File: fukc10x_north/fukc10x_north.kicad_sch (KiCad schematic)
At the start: 29 parts, among them J1 SM04B-SRSS-TB, J2 LED_Conn01x02_Pin, J3 LED_Conn01x02_Pin, J4 LED_Conn01x02_Pin, J5 LED_Conn01x02_Pin, J6 LED_Conn01x02_Pin, J7 LED_Conn01x02_Pin, J8 LED_Conn01x02_Pin, U1 XC6206P332MR, U2 STM32F072CBT6

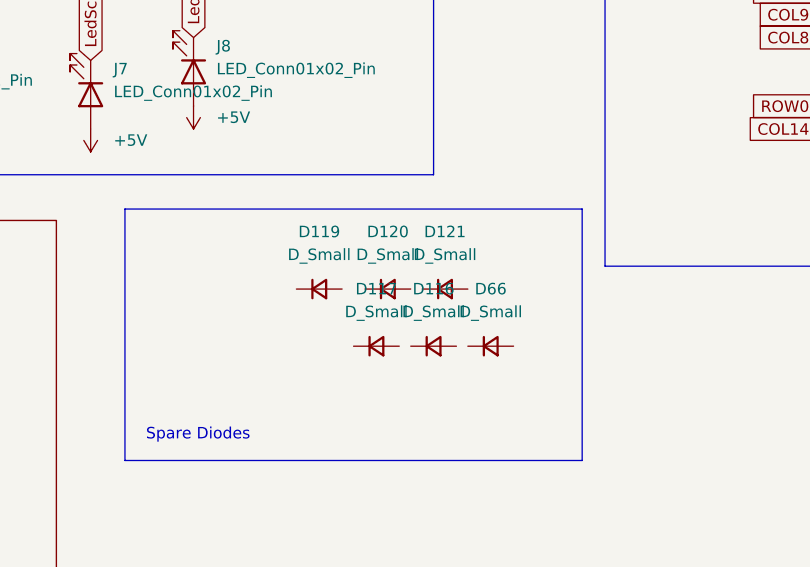
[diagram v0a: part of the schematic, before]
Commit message: updated parts for bom and stuff
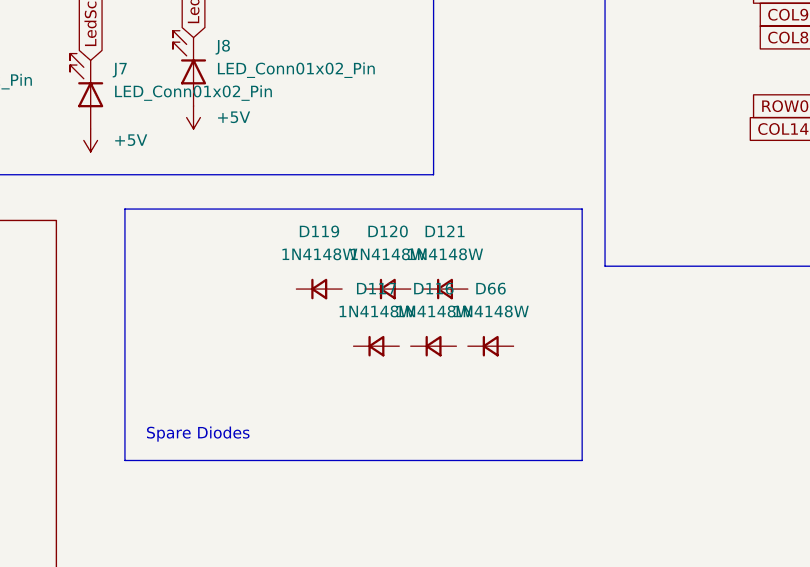
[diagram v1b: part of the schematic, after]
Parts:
- C10: MPN (none) -> CL05B104KO5NNNC
- D116, D117, D119, D120, D121, D66: value D_Small -> 1N4148W
- J2, J3, J4, J5, J6, J7, J8: now left out of the parts list

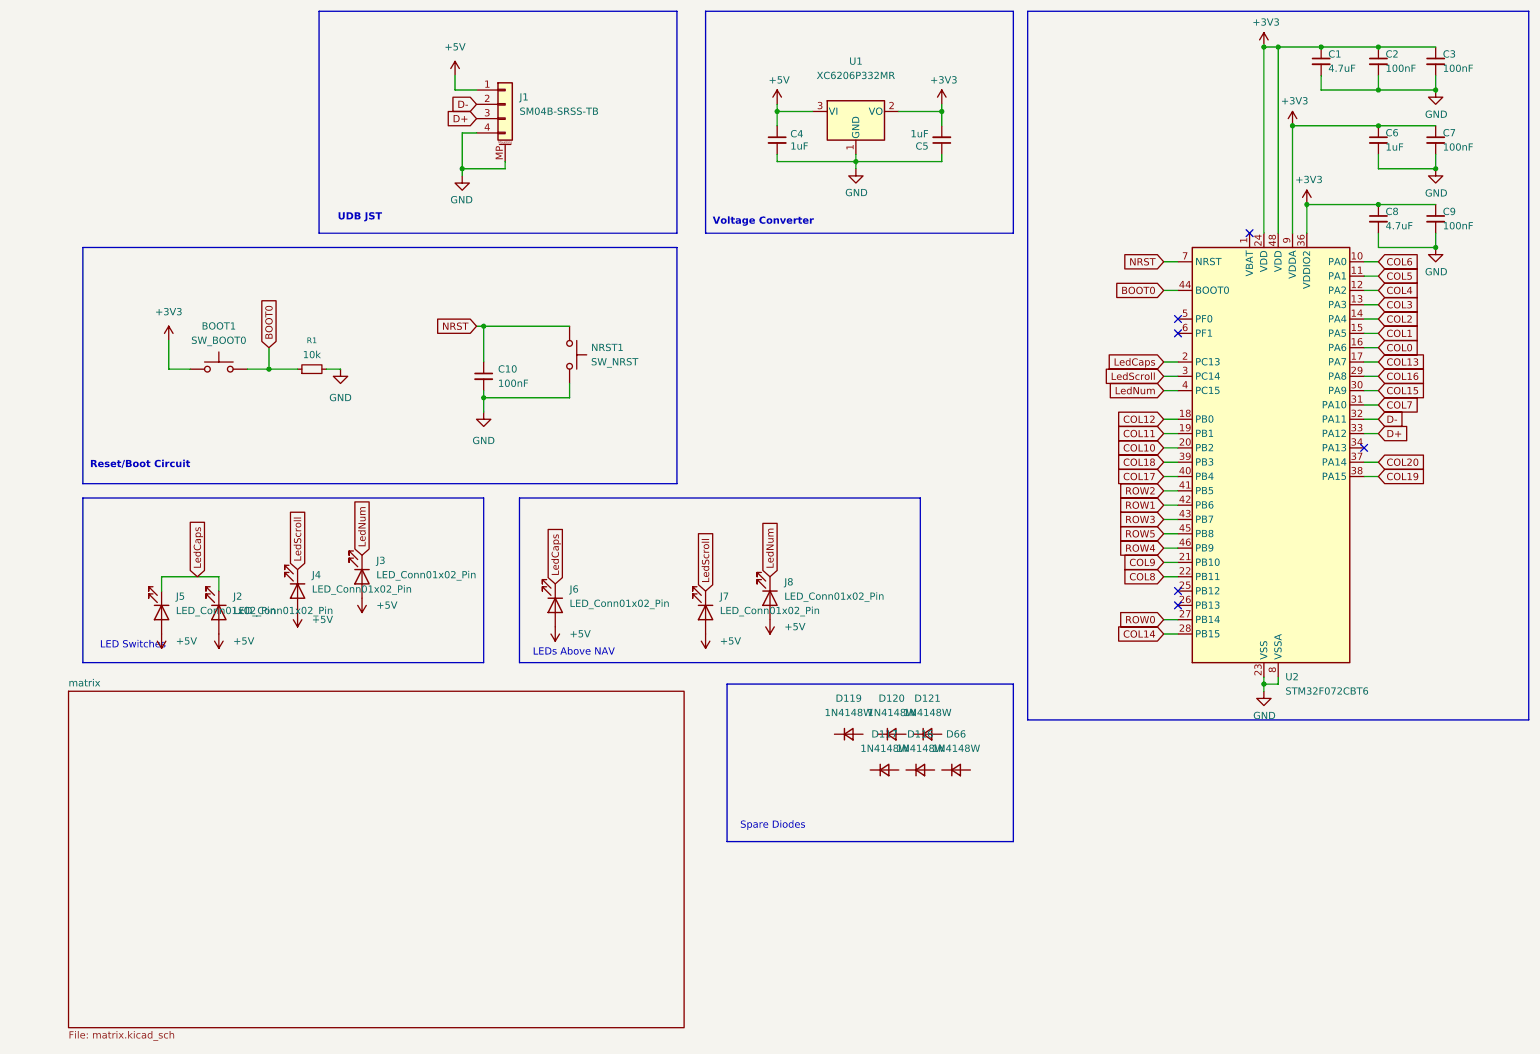
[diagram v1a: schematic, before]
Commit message: After feedback from gondo draining resistors and a crowbar diode added. Symbol for mcu changed to one from acheron project. Power/ground planes adjusted and added island around MCU for power and ground. Rerouted diodes adjusted trace widths.
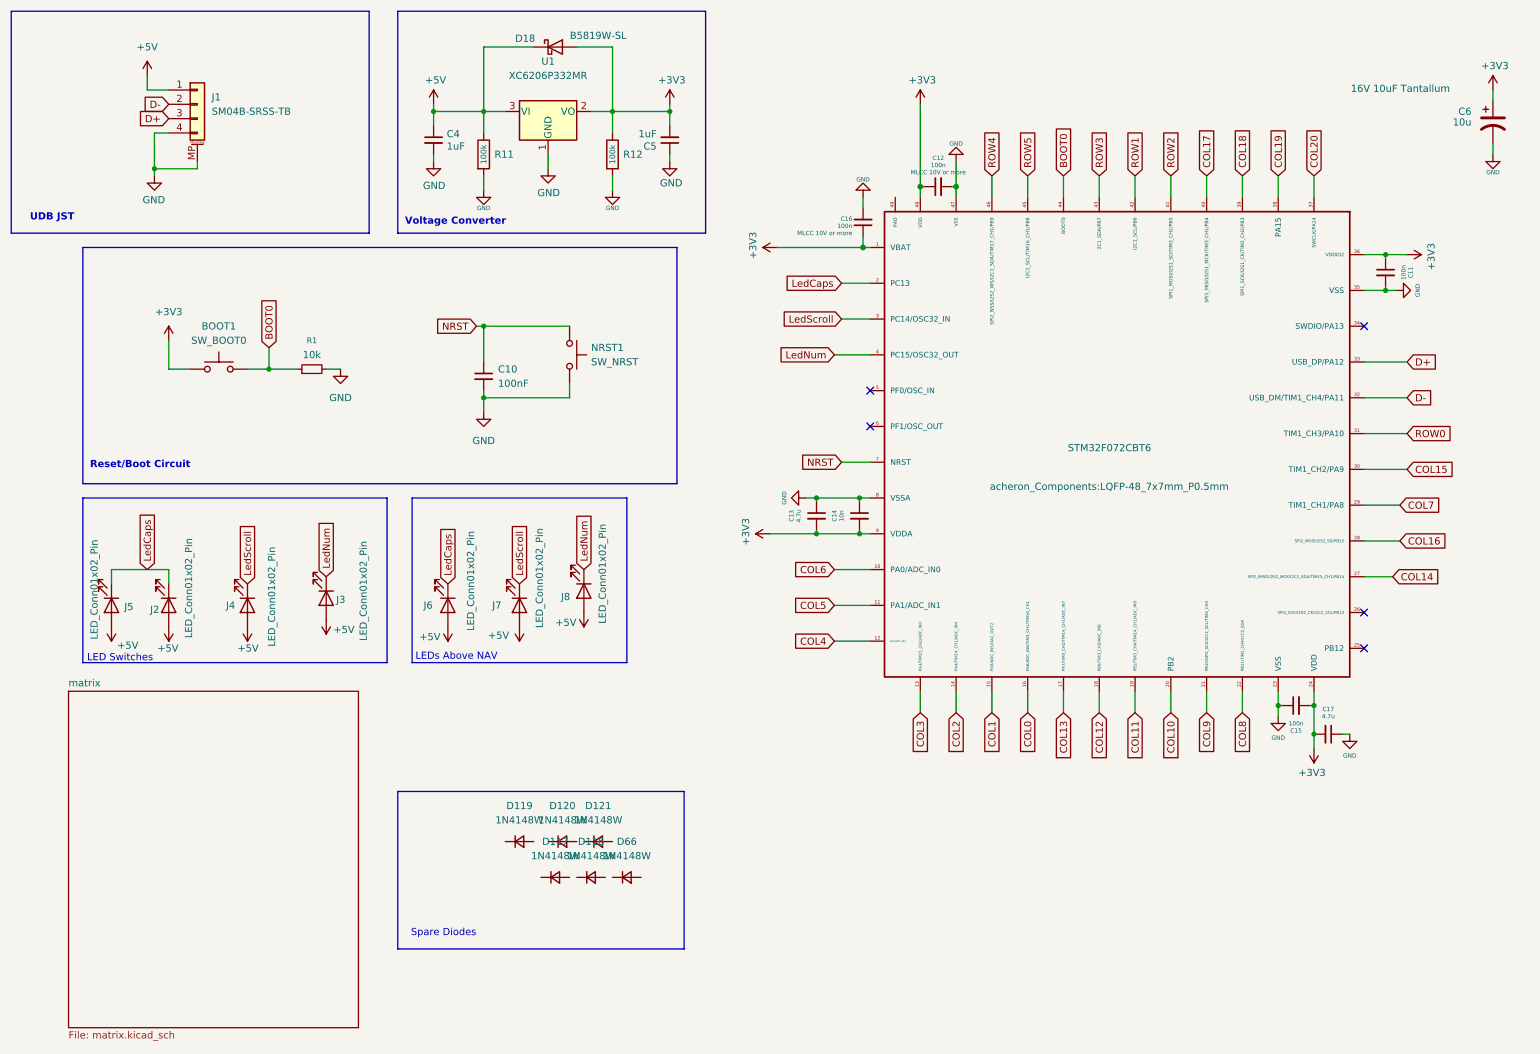
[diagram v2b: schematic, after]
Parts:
- removed C1, C8: 4.7uF, Capacitor_SMD:C_0402_1005Metric, symbol Device:C_Small
- removed C2, C3, C7, C9: 100nF, Capacitor_SMD:C_0402_1005Metric, symbol Device:C_Small
- removed C6: 1uF, Capacitor_SMD:C_0402_1005Metric, symbol Device:C_Small
- added C11, C12, C15, C16: 100n, Capacitor_SMD:C_0402_1005Metric, symbol Device:C_Small
- added C13, C17: 4.7u, Capacitor_SMD:C_0402_1005Metric, symbol Device:C_Small
- added C14: 10n, Capacitor_SMD:C_0402_1005Metric, symbol Device:C_Small
- added C6: 10u, acheron_Components:CP_EIA-3216-10_Kemet-I_Pad1.58x1.35mm_HandSolder, symbol Device:CP1
- added D18: B5819W-SL, acheron_Components:D_SOD-123, symbol Device:D_Schottky
- added R11, R12: 100k, Resistor_SMD:R_0805_2012Metric, symbol Device:R
- U2: footprint Package_QFP:LQFP-48_7x7mm_P0.5mm -> acheron_Components:LQFP-48_7x7mm_P0.5mm; symbol MCU_ST_STM32F0:STM32F072C8Tx -> Alexandria Acheron:STM32F072-UFQFPN48
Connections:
- net +3V3: now also U2.1 (VBAT), C11.1, C12.1, C13.2, C14.2, C15.2, C16.1, C17.2, C6.1, D18.2 (A), R12.1
- net +5V: now also D18.1 (K), R11.1
- net COL14: now also U2.27 (SPI2_MISO/I2S2_MCK/I2C2_SDA/TIM15_CH1/PB14); no longer U2.28 (PB15)
- net COL16: now also U2.28 (SPI2_MOSI/I2S2_SD/PB15); no longer U2.29 (PA8)
- net COL7: now also U2.29 (TIM1_CH1/PA8); no longer U2.31 (PA10)
- net GND: now also C11.2, C12.2, C13.1, C14.1, C15.1, C16.2, C17.1, C6.2, R11.2, R12.2
- net ROW0: now also U2.31 (TIM1_CH3/PA10); no longer U2.27 (PB14)
- no-connect marks 6 -> 5
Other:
- moved on the sheet: C4, C5, D116, D117, D119, D120, D121, D66, J1, J2, J3, J4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

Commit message: added library, fixed some routing and LED stuff
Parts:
- added Q1: AO3401A, acheron_Components:SOT-23, symbol Transistor_FET:AO3401A
- added Q2, Q3, Q4, Q5: 2N7002, acheron_Components:SOT-23, symbol Transistor_FET:2N7002
- added R10, R14, R15, R17, R5: 10k, Resistor_SMD:R_0402_1005Metric, symbol Device:R_Small
- added R11, R12, R16, R6, R9: 100, Resistor_SMD:R_0402_1005Metric, symbol Device:R_Small
- added R13, R4, R7, R8: 1k, Resistor_SMD:R_0402_1005Metric, symbol Device:R_Small
- J7: renamed from J2; value LED_Conn01x02_Pin -> LED
- renumbered C4 to C1, C15 to C10, C17 to C11, C5 to C2, C12 to C3, C6 to C4, C16 to C5, C11 to C6, C10 to C7, C13 to C8, C14 to C9, D18 to D1, D119 to D2, D120 to D3, D121 to D4, D117 to D5, D116 to D6, D66 to D7, J6 to J2, J7 to J3, J8 to J4, J3 to J5, J5 to J6, J4 to J8, R11 to R1, R12 to R2, R1 to R3
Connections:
- net +3V3: now also C11.1; no longer C11.2
- net +5V: now also Q1.2 (S), R5.2; no longer J2.2 (A), J3.2 (A), J4.2 (A), J5.2 (A), J6.2 (A), J7.2 (A), J8.2 (A)
- net COL0: now also U2.17 (PA7/TIM3_CH2/TIM14_CH1/ADC_IN7); no longer U2.16 (PA6/ADC_IN6/TIM3_CH1/TIM16_CH1)
- net COL1: now also U2.16 (PA6/ADC_IN6/TIM3_CH1/TIM16_CH1); no longer U2.15 (PA5/ADC_IN5/DAC_OUT2)
- net COL10: now also U2.21 (PB10/SPI2_SCK/I2C2_SCL/TIM2_CH3); no longer U2.20 (PB2)
- net COL11: now also U2.20 (PB2); no longer U2.19 (PB1/TIM3_CH4/TIM14_CH1/ADC_IN9)
- net COL12: now also U2.19 (PB1/TIM3_CH4/TIM14_CH1/ADC_IN9); no longer U2.18 (PB0/TIM3_CH3/ADC_IN8)
- net COL13: now also U2.18 (PB0/TIM3_CH3/ADC_IN8); no longer U2.17 (PA7/TIM3_CH2/TIM14_CH1/ADC_IN7)
- net COL2: now also U2.15 (PA5/ADC_IN5/DAC_OUT2); no longer U2.14 (PA4/TIM14_CH1/ADC_IN4)
- net COL3: now also U2.14 (PA4/TIM14_CH1/ADC_IN4); no longer U2.13 (PA3/TIM15_CH2/ADC_IN3)
- net COL8: now also U2.25 (PB12); no longer U2.22 (PB11/TIM2_CH4/I2C2_SDA)
- net COL9: now also U2.22 (PB11/TIM2_CH4/I2C2_SDA); no longer U2.21 (PB10/SPI2_SCK/I2C2_SCL/TIM2_CH3)
- net GND: now also C11.2, Q2.2 (S), Q3.2 (S), Q4.2 (S), Q5.2 (S), R10.1, R14.1, R15.1, R17.1; no longer C11.1
- net LedCaps: now also R11.1; no longer J2.1 (K), J6.1 (K), J7.1 (K)
- net LedNum: now also R12.1; no longer J4.1 (K), J5.1 (K)
- net LedScroll: now also R16.1; no longer J3.1 (K), J8.1 (K)
- new net: Q2.3 (D), R5.1, R6.1
- new net: Q1.1 (G), R6.2
- new net: Q5.1 (G), R16.2, R17.2
- new net: J4.1 (K), J5.1 (K), Q4.3 (D)
- new net: J5.2 (A), R8.1
- new net: Q4.1 (G), R12.2, R15.2
- new net: Q3.1 (G), R11.2, R14.2
- new net: J2.1 (K), J6.1 (K), J7.1 (K), Q3.3 (D)
- new net: J2.2 (A), J3.2 (A), J4.2 (A), R4.1
- new net: J3.1 (K), J8.1 (K), Q5.3 (D)
- new net: J8.2 (A), R13.1
- new net: Q2.1 (G), R10.2, R9.2
- new net: J6.2 (A), J7.2 (A), R7.1
- new net LED_PWM: R9.1, U2.13 (PA3/TIM15_CH2/ADC_IN3)
- new net LED_PWM_OUT: Q1.3 (D), R13.2, R4.2, R7.2, R8.2
- no-connect marks 5 -> 4
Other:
- note removed: "LEDs Above NAV"
- moved on the sheet: C10, C11, C3, C4, C5, C6, C8, C9, D2, D3, D4, D5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

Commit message: adjusted some traces, fixed some stuff for the leds. Reset and boot circutry still pending. Full DRC ran and mostly fixed
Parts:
- removed BOOT1: SW_BOOT0, Button_Switch_SMD:SW_SPST_TL3342, symbol Switch:SW_Push
- removed C7: 100nF, Capacitor_SMD:C_0402_1005Metric, symbol Device:C_Small
- removed NRST1: SW_NRST, Button_Switch_SMD:SW_SPST_TL3342, symbol Switch:SW_Push
- removed R3: 10k, Resistor_SMD:R_0402_1005Metric, symbol Device:R_Small
- added R18, R19: 1k, Resistor_SMD:R_0402_1005Metric, symbol Device:R_Small
- Q1, Q2, Q3, Q4, Q5: footprint acheron_Components:SOT-23 -> Package_TO_SOT_SMD:SOT-23
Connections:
- net COL15: now also U2.13 (PA3/TIM15_CH2/ADC_IN3); no longer U2.30 (TIM1_CH2/PA9)
- net COL16: now also U2.25 (PB12); no longer U2.28 (SPI2_MOSI/I2S2_SD/PB15)
- net COL8: now also U2.28 (SPI2_MOSI/I2S2_SD/PB15); no longer U2.25 (PB12)
- net LED_PWM: now also U2.30 (TIM1_CH2/PA9); no longer U2.13 (PA3/TIM15_CH2/ADC_IN3)
- net LED_PWM_OUT: now also R18.2, R19.2
- net at J2.2 (A), R4.1: no longer J3.2 (A), J4.2 (A)
- new net: J3.2 (A), R18.1
- new net: J4.2 (A), R19.1
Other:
- moved on the sheet: J2, J3, J4, J5, J6, J7, J8, Q3, Q4, Q5, R11, R12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
